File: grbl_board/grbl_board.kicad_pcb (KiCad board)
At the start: 4 copper layers, 138.4 x 138.3 mm, 236 parts, among them J1 COOL, J10 DOOR, J11 PROBE, J12 INP, J13 LIM, J14 24V_VFD, J15 Spindle, J16 freq, J17 USB_B, J18 ICSP, J2 12VDC, J3 USB_B, J4 ICSP, J5 Screw_Terminal_01x04, J6 X_STEPPER, J7 Y_STEPPER, J8 Z_STEPPER, J9 E_STEPPER, Q1 BSS127S, Q2 BSS127S, Q3 ZVN4306GTA, Q4 IRF9Z24SPBF, Q5 BSS127S, Q6 BSS127S, Q7 BSS127S, SW1 SW_Push, SW2 SW_Push, U1 FT231XS, U10 6N137, U11 6N137, U12 6N137, U13 6N137, U14 6N137, U15 6N137, U16 6N137, U17 6N137, U18 6N137, U19 6N137, U2 ATmega2560-16AU, U20 6N137, U21 BD9G341EFJ, U22 LMV358, U23 OPA2192, U24 L7805, U25 FT231XS, U26 40106, U27 74LS155, U28 ATmega328P-AU, U29 74LS153, U3 LT1962-5, U30 74LS153, U4 BD9G341EFJ, U5 TMC5160_SILENTSTEPSTICK, U6 TMC5160_SILENTSTEPSTICK, U7 TMC5160_SILENTSTEPSTICK, U8 TMC5160_SILENTSTEPSTICK, U9 6N137, Y1 16M, Y2 16M

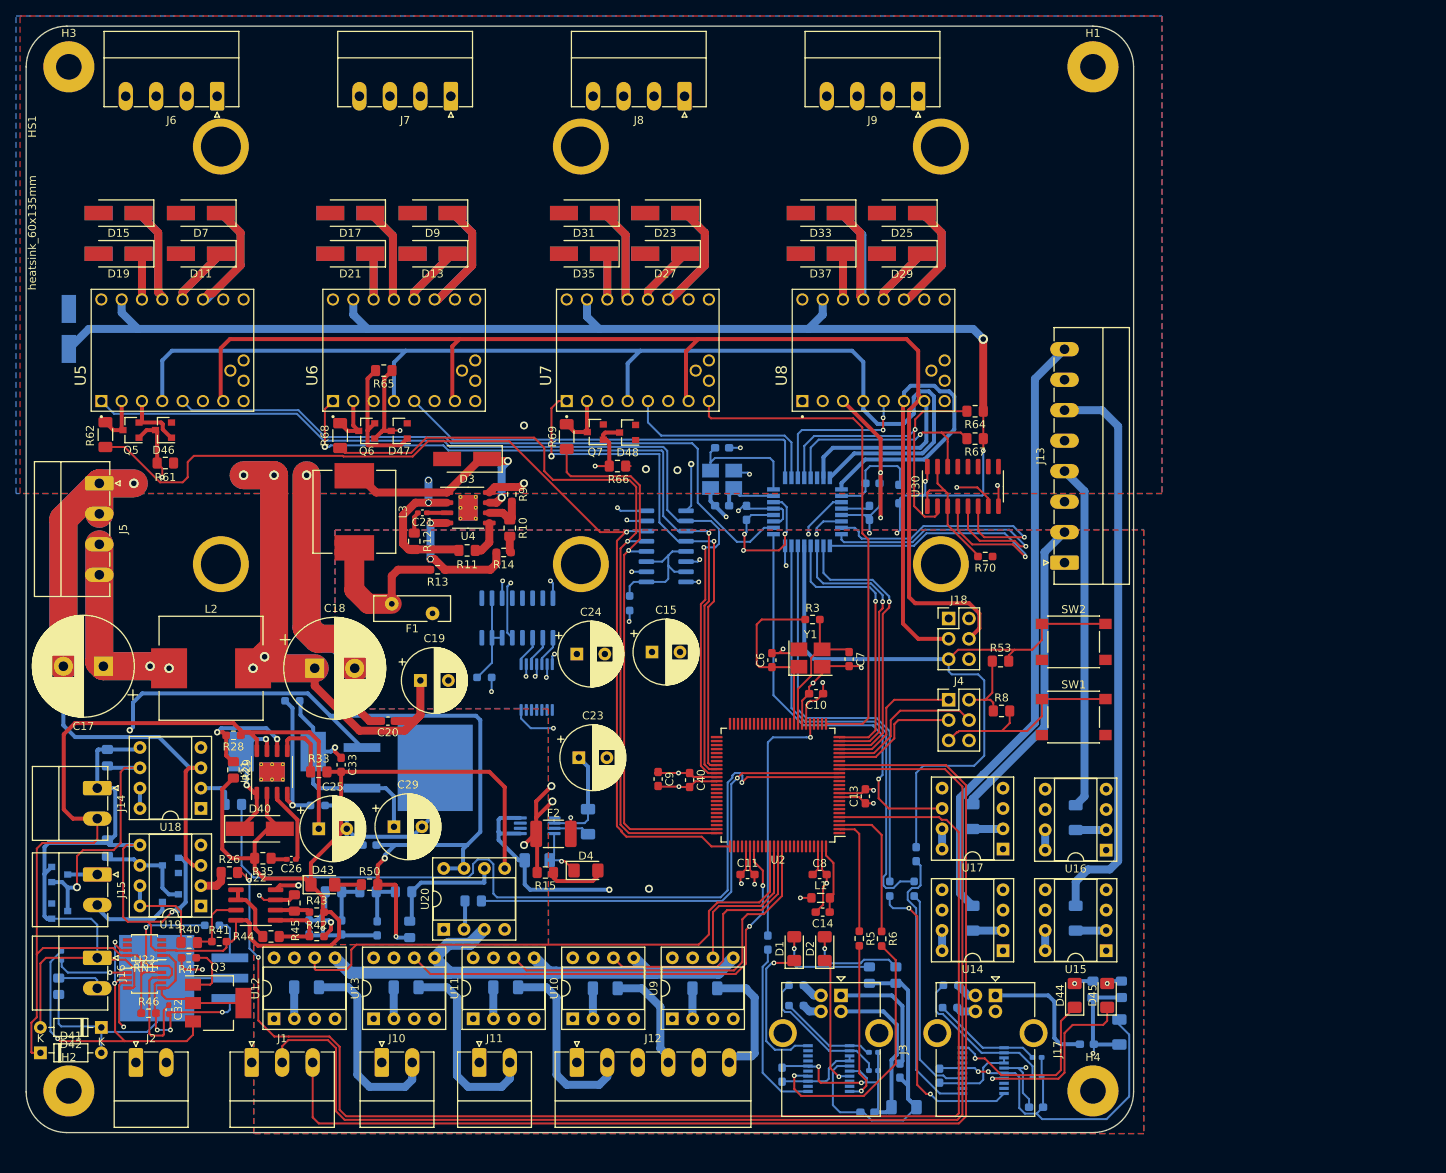
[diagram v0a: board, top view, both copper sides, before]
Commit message: added connector labels and tmc 3d model
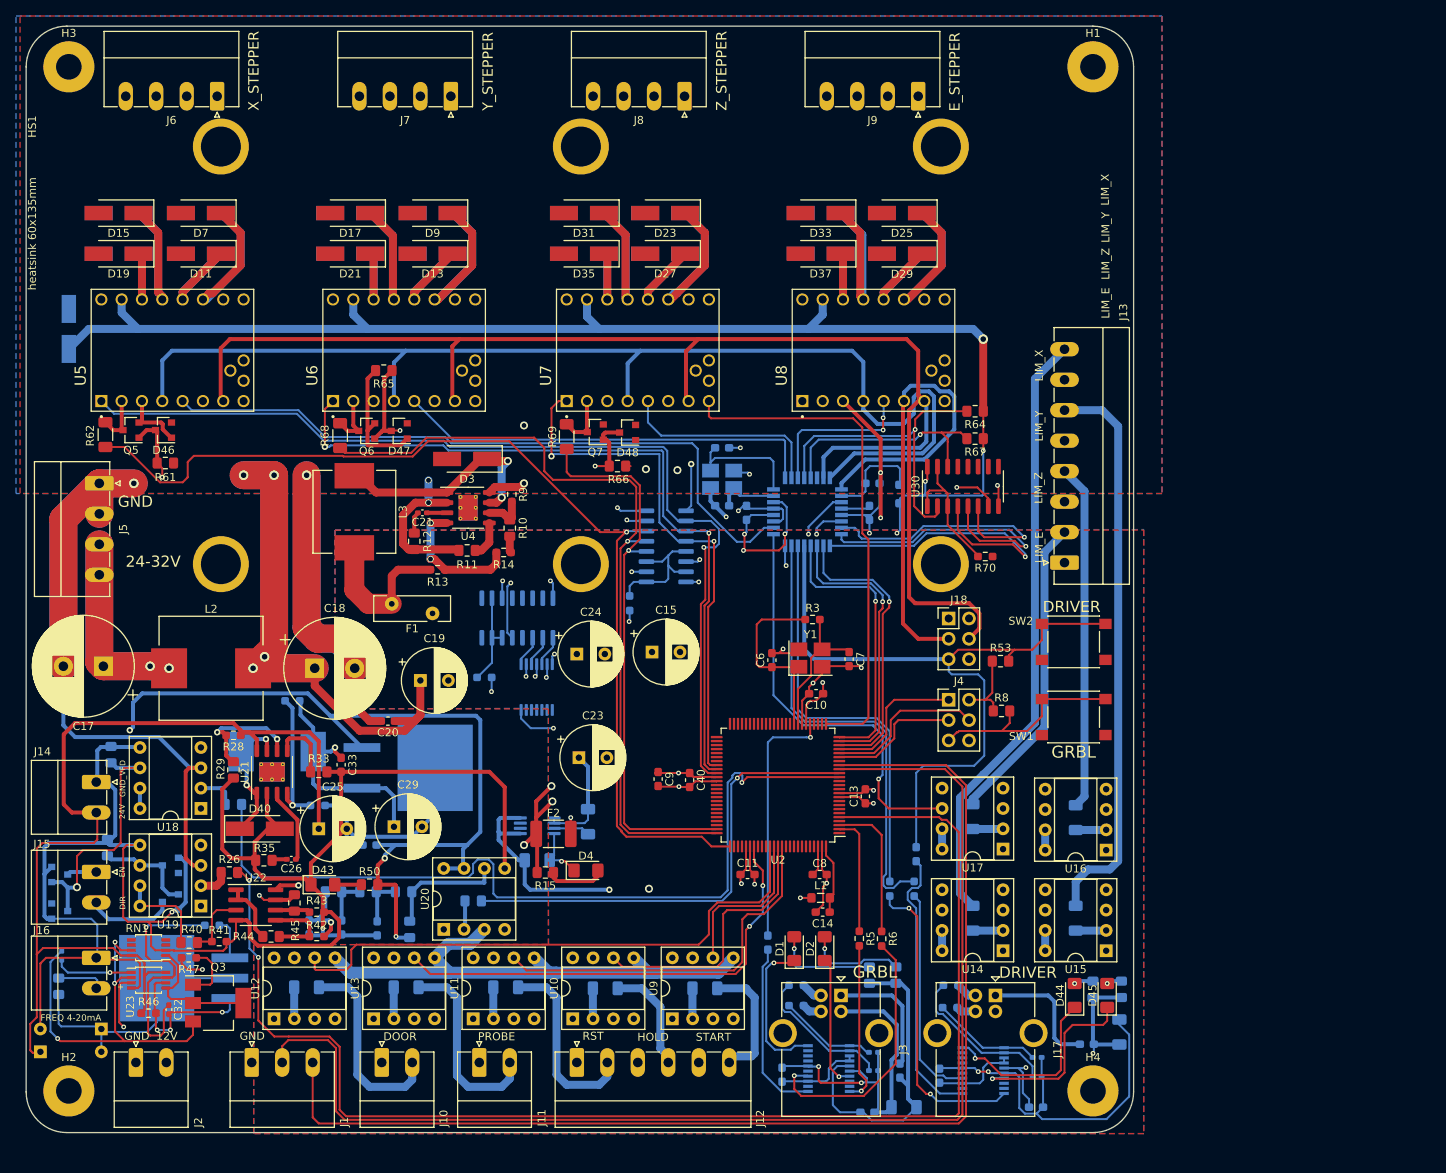
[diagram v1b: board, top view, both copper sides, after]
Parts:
- D41, D42: moved to B.Cu
- HS1: value heatsink_60x135mm -> heatsink 60x135mm
- moved J14 0.77 mm to (48.1, 114.8)
- moved R31 0.59 mm to (50.0, 111.4)
- moved RN1 0.51 mm to (54.7, 135.5)
- moved U23 0.51 mm to (54.7, 139.6)
- moved J15 0.34 mm to (48.1, 126.0)
- moved R35 0.28 mm to (69.1, 124.6)
- moved D42 0.19 mm to (48.8, 145.7)
- moved D41 0.13 mm to (41.1, 148.5)
- moved J16 0.13 mm to (48.1, 136.8)
- moved R32 0.06 mm to (49.5, 123.0)
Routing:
- net Net-(J3-Pad5): track 0.00 -> 12.0 mm
- net Net-(J17-Pad5): track 0.00 -> 12.0 mm
- net /spinlde_cntrl/GND_VFD: track 267.8 -> 268.6 mm
- net Net-(C31-Pad2): track 24.9 -> 25.7 mm
- net Net-(Q3-Pad2): track 17.9 -> 17.3 mm
- net Net-(R45-Pad1): track 44.4 -> 44.9 mm
- net Net-(C31-Pad1): track 47.8 -> 48.3 mm
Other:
- board text added: "+"
- board text added: "-"
- board text added: "12V"
- board text added: "24-32V"
- board text added: "24V"
- board text added: "DIR"
- board text added: "DOOR"
- board text added: "DRIVER"
- board text added: "EN"
- board text added: "E_STEPPER"
- board text added: "FREQ 4-20mA"
- board text added: "GND"
- board text added: "GND_VFD"
- board text added: "GRBL"
- board text added: "HOLD"
- board text added: "LIM_E"
- board text added: "LIM_X"
- board text added: "LIM_Y"
- board text added: "LIM_Z"
- board text added: "PROBE"
- board text added: "RST"
- board text added: "START"
- board text added: "X_STEPPER"
- board text added: "Y_STEPPER"
- board text added: "Z_STEPPER"

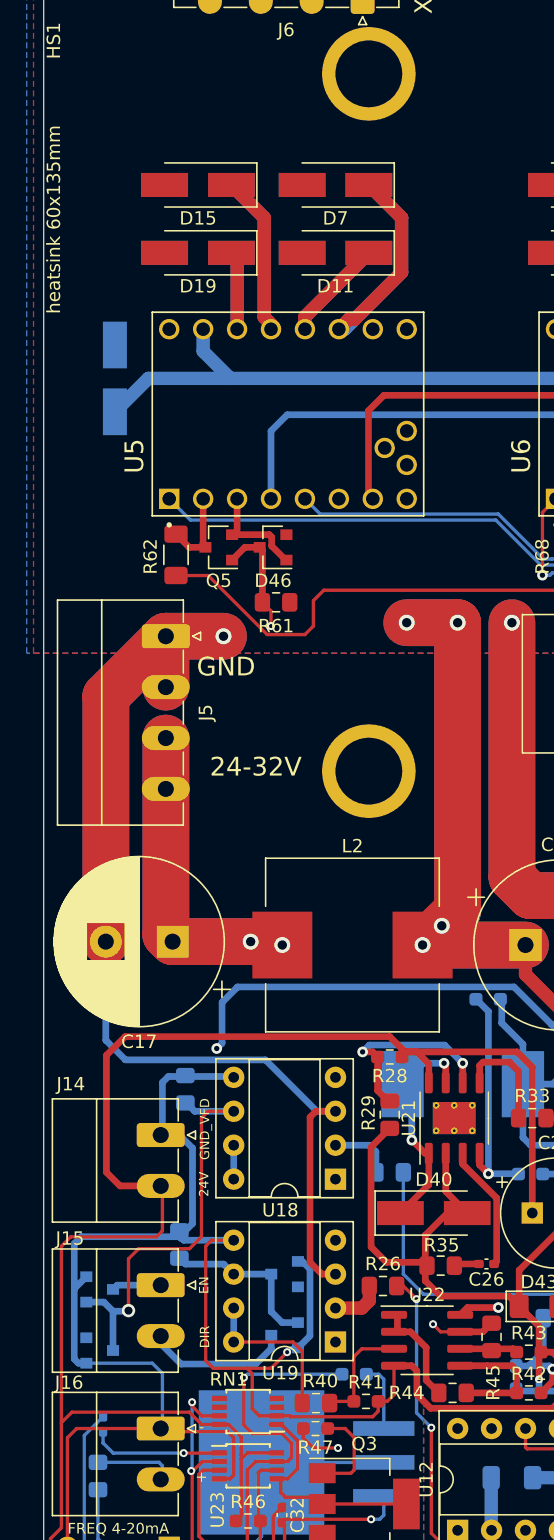
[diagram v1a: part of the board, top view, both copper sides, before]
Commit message: added usb 3d model and fixed footprint associations
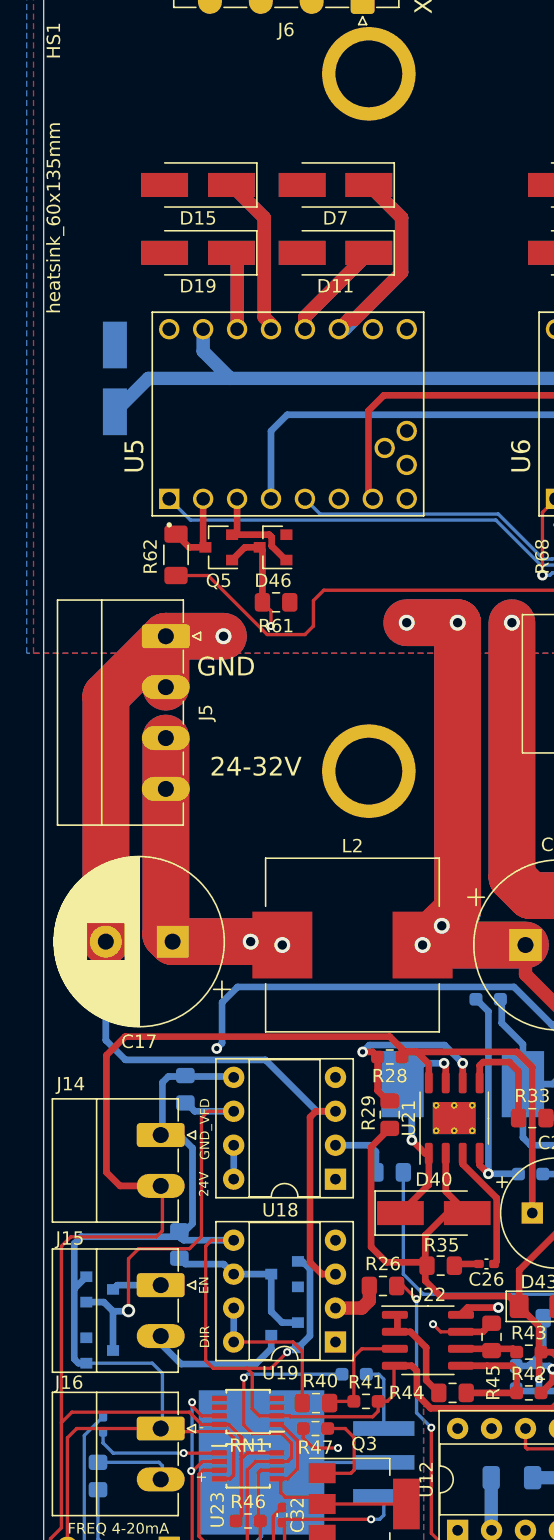
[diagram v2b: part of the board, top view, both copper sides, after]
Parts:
- HS1: value heatsink 60x135mm -> heatsink_60x135mm
- J17, J3: footprint Connector_USB:USB_B_OST_USB-B1HSxx_Horizontal -> grbl_board:USB_B_OST_USB-B1HSxx_Horizontal
- moved U22 0.06 mm to (68.1, 130.2)
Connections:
- U27 pad 16: Net-(U27-Pad16) -> +5V
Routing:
- net Net-(Q3-Pad2): track 17.3 -> 16.8 mm

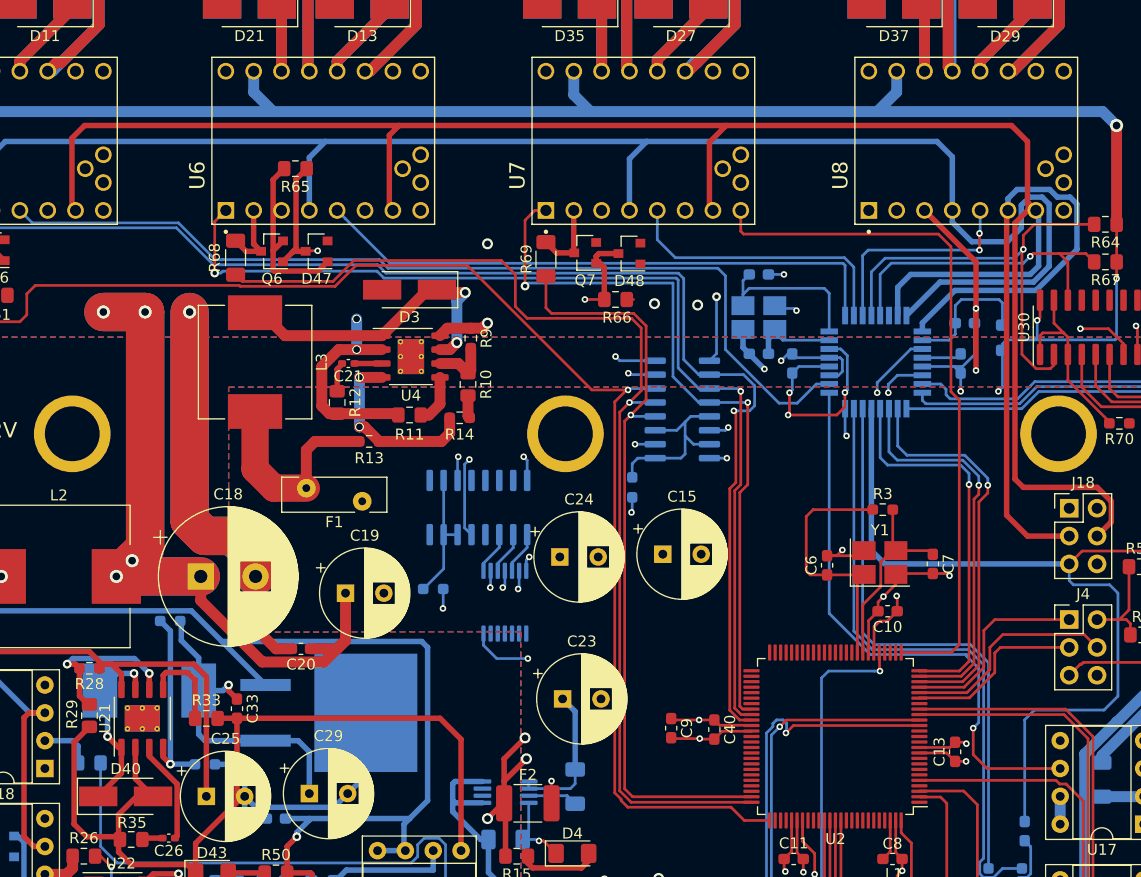
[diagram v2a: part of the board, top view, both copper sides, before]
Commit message: added more filtering caps
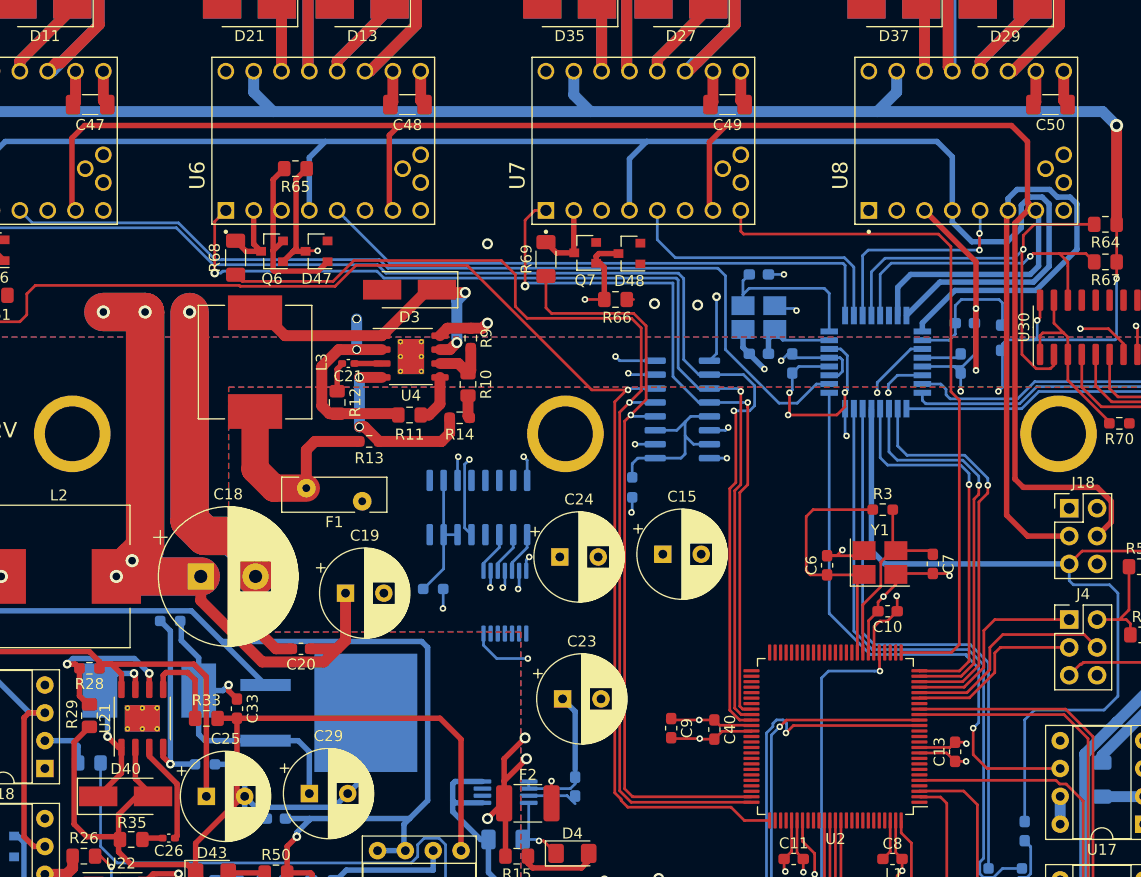
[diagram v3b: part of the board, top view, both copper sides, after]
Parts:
- added C47: 4.7u, Capacitor_SMD:C_1206_3216Metric_Pad1.33x1.80mm_HandSolder, F.Cu at (65.3, 57.5)
- added C48: 4.7u, Capacitor_SMD:C_1206_3216Metric_Pad1.33x1.80mm_HandSolder, F.Cu at (94.3, 57.5)
- added C49: 4.7u, Capacitor_SMD:C_1206_3216Metric_Pad1.33x1.80mm_HandSolder, F.Cu at (123.5, 57.5)
- added C50: 4.7u, Capacitor_SMD:C_1206_3216Metric_Pad1.33x1.80mm_HandSolder, F.Cu at (153.0, 57.5)
- C22: footprint Capacitor_SMD:C_1206_3216Metric_Pad1.33x1.80mm_HandSolder -> Capacitor_SMD:C_0603_1608Metric_Pad1.08x0.95mm_HandSolder
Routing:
- net /VMOT: track 205.0 -> 217.7 mm
- net GND: track 706.8 -> 719.4 mm
